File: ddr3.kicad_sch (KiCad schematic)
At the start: 26 parts, among them U11 LIFCL-40-9BG256C, U12 MT41K128M16JT-125_K

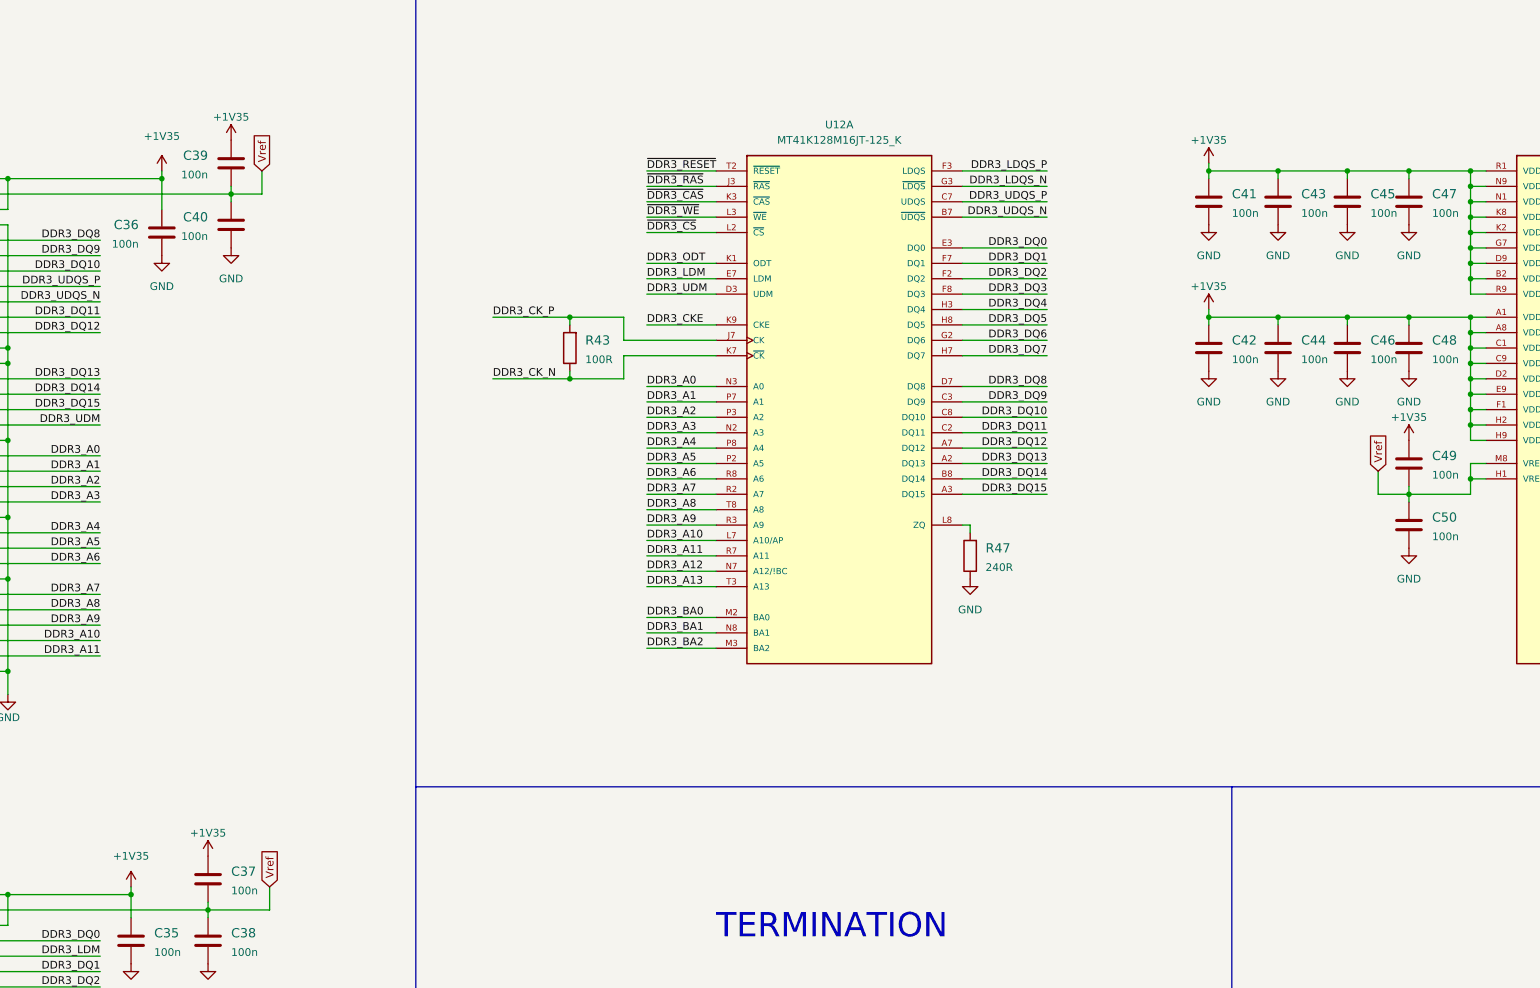
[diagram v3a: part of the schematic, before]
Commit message: Switched voltages to support DDR3 and RPC memories
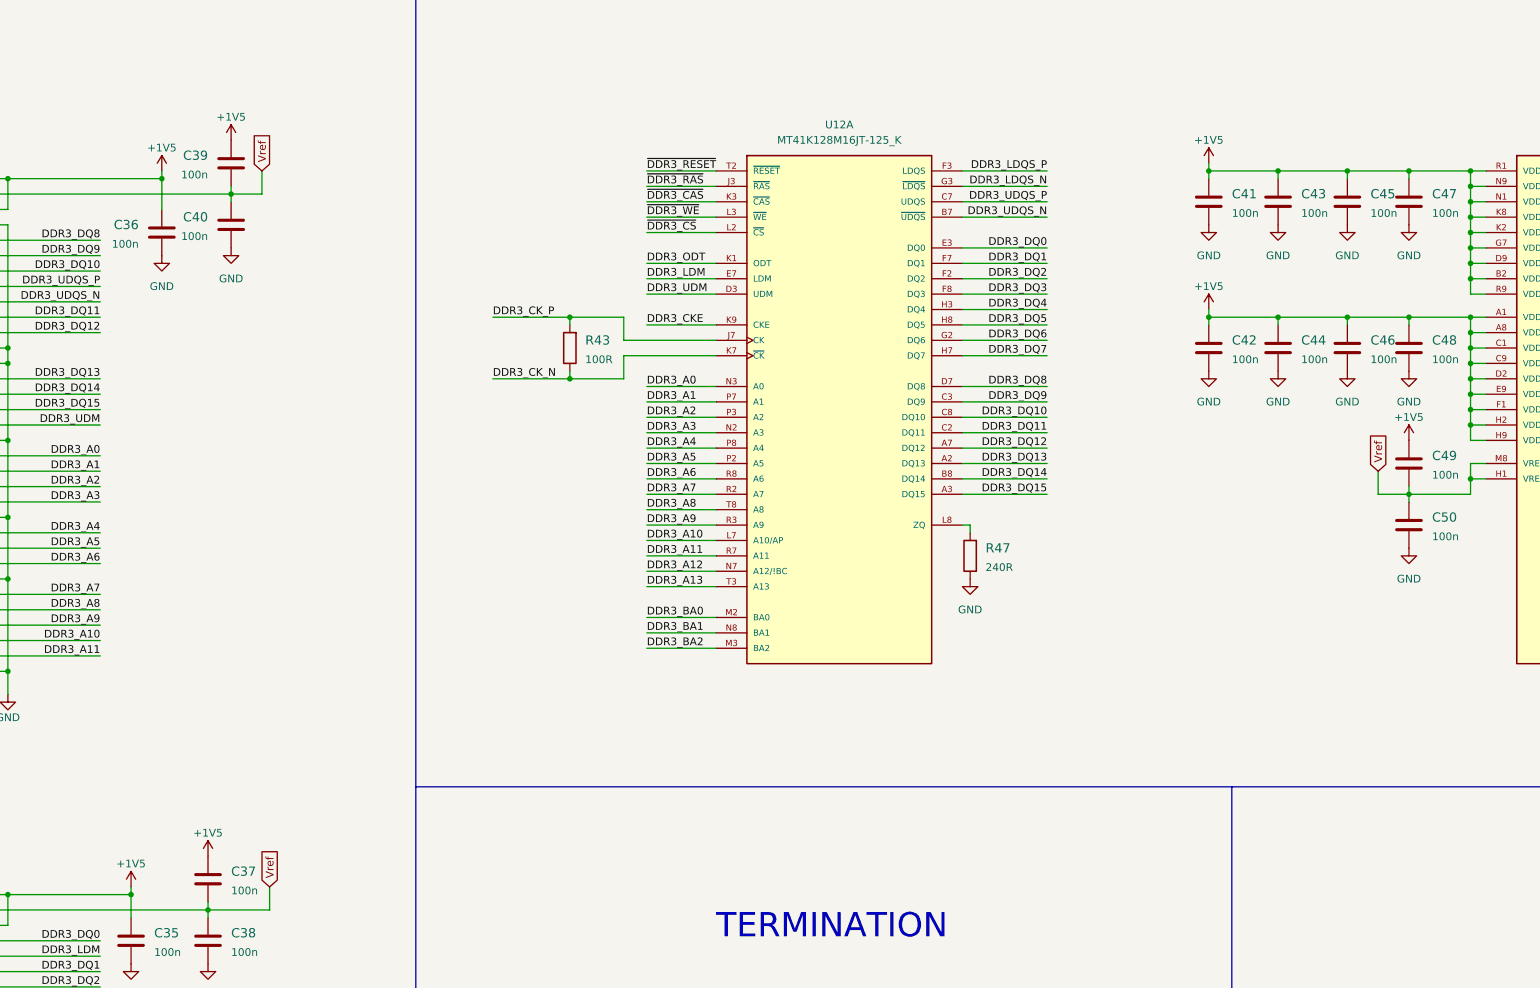
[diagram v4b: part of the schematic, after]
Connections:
- net +1V35 renamed +1V5
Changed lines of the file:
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@@
   (junction (at 269.24 207.01) (diameter 0) (color 0 0 0 0)
   )
-  (junction (at 295.91 78.74) (diameter 0) (color 0 0 0 0)
-  )
   (junction (at 226.06 209.55) (diameter 0) (color 0 0 0 0)
   )
@@
   (junction (at 339.09 54.61) (diameter 0) (color 0 0 0 0)
   )
+  (junction (at 295.91 78.74) (diameter 0) (color 0 0 0 0)
+  )
   (junction (at 269.24 226.06) (diameter 0) (color 0 0 0 0)
   )
@@
     (stroke (width 0) (type default) (color 0 0 0 0))
   )
+  (wire (pts (xy 295.91 77.47) (xy 295.91 78.74))
+    (stroke (width 0) (type default) (color 0 0 0 0))
+  )
   (wire (pts (xy 382.27 62.23) (xy 384.81 62.23))
     (stroke (width 0) (type default) (color 0 0 0 0))
@@
     (stroke (width 0) (type default) (color 0 0 0 0))
   )
-  (wire (pts (xy 295.91 77.47) (xy 295.91 78.74))
-    (stroke (width 0) (type default) (color 0 0 0 0))
-  )
   (wire (pts (xy 269.24 92.71) (xy 255.27 92.71))
     (stroke (width 0) (type default) (color 0 0 0 0))
@@
     (pin "2")
   )
-  (symbol (lib_id "power:+1V35") (at 295.91 77.47 0) (unit 1)
-    (in_bom yes) (on_board yes)
-    (property "Reference" "#PWR094" (id 0) (at 295.91 81.28 0)
-      (effects (font (size 1.27 1.27)) hide)
-    )
-    (property "Value" "+1V35" (id 1) (at 295.91 73.66 0))
-    (property "Footprint" "crosslink-nx-video-converter-footprints:" (id 2) (at 295.91 77.47 0)
-      (effects (font (size 1.27 1.27)) hide)
-    )
-    (property "Datasheet" "" (id 3) (at 295.91 77.47 0)
-      (effects (font (size 1.27 1.27)) hide)
-    )
-    (pin "1")
-  )
   (symbol (lib_id "power:GND") (at 307.34 63.5 0) (unit 1)
     (in_bom yes) (on_board yes) (fields_autoplaced)
@@
     (pin "8")
   )
-  (symbol (lib_id "power:+1V35") (at 328.93 99.06 0) (unit 1)
-    (in_bom yes) (on_board yes)
-    (property "Reference" "#PWR0102" (id 0) (at 328.93 102.87 0)
-      (effects (font (size 1.27 1.27)) hide)
-    )
-    (property "Value" "+1V35" (id 1) (at 328.93 95.25 0))
-    (property "Footprint" "crosslink-nx-video-converter-footprints:" (id 2) (at 328.93 99.06 0)
-      (effects (font (size 1.27 1.27)) hide)
-    )
-    (property "Datasheet" "" (id 3) (at 328.93 99.06 0)
-      (effects (font (size 1.27 1.27)) hide)
-    )
-    (pin "1")
-  )
   (symbol (lib_id "crosslink-nx-video-converter:R_100R_0402") (at 190.5 83.82 90) (unit 1)
     (in_bom yes) (on_board yes) (fields_autoplaced)
@@
     (pin "2")
   )
+  (symbol (lib_id "power:+1V5") (at 118.11 172.72 0) (unit 1)
+    (in_bom yes) (on_board yes)
+    (property "Reference" "#PWR0229" (id 0) (at 118.11 176.53 0)
+      (effects (font (size 1.27 1.27)) hide)
+    )
+    (property "Value" "+1V5" (id 1) (at 118.11 168.91 0))
+    (property "Footprint" "" (id 2) (at 118.11 172.72 0)
+      (effects (font (size 1.27 1.27)) hide)
+    )
+    (property "Datasheet" "" (id 3) (at 118.11 172.72 0)
+      (effects (font (size 1.27 1.27)) hide)
+    )
+    (pin "1")
+  )
   (symbol (lib_id "power:GND") (at 295.91 63.5 0) (unit 1)
     (in_bom yes) (on_board yes) (fields_autoplaced)
@@
     (pin "8")
   )
-  (symbol (lib_id "power:+1V35") (at 123.19 54.61 0) (mirror y) (unit 1)
-    (in_bom yes) (on_board yes) (fields_autoplaced)
-    (property "Reference" "#PWR085" (id 0) (at 123.19 58.42 0)
-      (effects (font (size 1.27 1.27)) hide)
-    )
-    (property "Value" "+1V35" (id 1) (at 123.19 48.895 0))
-    (property "Footprint" "crosslink-nx-video-converter-footprints:" (id 2) (at 123.19 54.61 0)
-      (effects (font (size 1.27 1.27)) hide)
-    )
-    (property "Datasheet" "" (id 3) (at 123.19 54.61 0)
-      (effects (font (size 1.27 1.27)) hide)
-    )
-    (pin "1")
-  )
   (symbol (lib_id "power:GND") (at 295.91 87.63 0) (unit 1)
     (in_bom yes) (on_board yes) (fields_autoplaced)
@@
     (pin "2")
   )
-  (symbol (lib_id "power:+1V35") (at 130.81 167.64 0) (mirror y) (unit 1)
+  (symbol (lib_id "power:+1V5") (at 130.81 167.64 0) (unit 1)
     (in_bom yes) (on_board yes)
-    (property "Reference" "#PWR087" (id 0) (at 130.81 171.45 0)
+    (property "Reference" "#PWR0230" (id 0) (at 130.81 171.45 0)
       (effects (font (size 1.27 1.27)) hide)
     )
-    (property "Value" "+1V35" (id 1) (at 130.81 163.83 0))
-    (property "Footprint" "crosslink-nx-video-converter-footprints:" (id 2) (at 130.81 167.64 0)
+    (property "Value" "+1V5" (id 1) (at 130.81 163.83 0))
+    (property "Footprint" "" (id 2) (at 130.81 167.64 0)
       (effects (font (size 1.27 1.27)) hide)
     )
@@
     (pin "2")
   )
+  (symbol (lib_id "power:+1V5") (at 134.62 49.53 0) (unit 1)
+    (in_bom yes) (on_board yes)
+    (property "Reference" "#PWR0231" (id 0) (at 134.62 53.34 0)
+      (effects (font (size 1.27 1.27)) hide)
+    )
+    (property "Value" "+1V5" (id 1) (at 134.62 45.72 0))
+    (property "Footprint" "" (id 2) (at 134.62 49.53 0)
+      (effects (font (size 1.27 1.27)) hide)
+    )
+    (property "Datasheet" "" (id 3) (at 134.62 49.53 0)
+      (effects (font (size 1.27 1.27)) hide)
+    )
+    (pin "1")
+  )
   (symbol (lib_id "crosslink-nx-video-converter:C_100n_0402") (at 307.34 59.69 0) (unit 1)
     (in_bom yes) (on_board yes) (fields_autoplaced)
@@
     (pin "2")
   )
+  (symbol (lib_id "power:+1V5") (at 328.93 99.06 0) (unit 1)
+    (in_bom yes) (on_board yes)
+    (property "Reference" "#PWR0234" (id 0) (at 328.93 102.87 0)
+      (effects (font (size 1.27 1.27)) hide)
+    )
+    (property "Value" "+1V5" (id 1) (at 328.93 95.25 0))
+    (property "Footprint" "" (id 2) (at 328.93 99.06 0)
+      (effects (font (size 1.27 1.27)) hide)
+    )
+    (property "Datasheet" "" (id 3) (at 328.93 99.06 0)
+      (effects (font (size 1.27 1.27)) hide)
+    )
+    (pin "1")
+  )
   (symbol (lib_id "power:GND") (at 118.11 185.42 0) (unit 1)
     (in_bom yes) (on_board yes) (fields_autoplaced)
@@
     (pin "1")
   )
-  (symbol (lib_id "power:+1V35") (at 118.11 172.72 0) (mirror y) (unit 1)
-    (in_bom yes) (on_board yes)
-    (property "Reference" "#PWR083" (id 0) (at 118.11 176.53 0)
-      (effects (font (size 1.27 1.27)) hide)
-    )
-    (property "Value" "+1V35" (id 1) (at 118.11 167.64 0))
-    (property "Footprint" "crosslink-nx-video-converter-footprints:" (id 2) (at 118.11 172.72 0)
-      (effects (font (size 1.27 1.27)) hide)
-    )
-    (property "Datasheet" "" (id 3) (at 118.11 172.72 0)
-      (effects (font (size 1.27 1.27)) hide)
-    )
-    (pin "1")
-  )
   (symbol (lib_id "power:GND") (at 97.79 140.97 0) (mirror y) (unit 1)
     (in_bom yes) (on_board yes)
@@
     (pin "2")
   )
-  (symbol (lib_id "power:+1V35") (at 295.91 53.34 0) (unit 1)
-    (in_bom yes) (on_board yes)
-    (property "Reference" "#PWR092" (id 0) (at 295.91 57.15 0)
-      (effects (font (size 1.27 1.27)) hide)
-    )
-    (property "Value" "+1V35" (id 1) (at 295.91 49.53 0))
-    (property "Footprint" "crosslink-nx-video-converter-footprints:" (id 2) (at 295.91 53.34 0)
-      (effects (font (size 1.27 1.27)) hide)
-    )
-    (property "Datasheet" "" (id 3) (at 295.91 53.34 0)
-      (effects (font (size 1.27 1.27)) hide)
-    )
-    (pin "1")
-  )
   (symbol (lib_id "power:GND") (at 307.34 87.63 0) (unit 1)
     (in_bom yes) (on_board yes) (fields_autoplaced)
@@
     (pin "8")
   )
-  (symbol (lib_id "power:+1V35") (at 134.62 49.53 0) (mirror y) (unit 1)
-    (in_bom yes) (on_board yes)
-    (property "Reference" "#PWR089" (id 0) (at 134.62 53.34 0)
-      (effects (font (size 1.27 1.27)) hide)
-    )
-    (property "Value" "+1V35" (id 1) (at 134.62 45.72 0))
-    (property "Footprint" "crosslink-nx-video-converter-footprints:" (id 2) (at 134.62 49.53 0)
-      (effects (font (size 1.27 1.27)) hide)
-    )
-    (property "Datasheet" "" (id 3) (at 134.62 49.53 0)
-      (effects (font (size 1.27 1.27)) hide)
-    )
-    (pin "1")
-  )
   (symbol (lib_id "power:GND") (at 328.93 63.5 0) (unit 1)
     (in_bom yes) (on_board yes) (fields_autoplaced)
@@
     (pin "1")
   )
+  (symbol (lib_id "power:+1V5") (at 295.91 77.47 0) (unit 1)
+    (in_bom yes) (on_board yes)
+    (property "Reference" "#PWR0233" (id 0) (at 295.91 81.28 0)
+      (effects (font (size 1.27 1.27)) hide)
+    )
+    (property "Value" "+1V5" (id 1) (at 295.91 73.66 0))
+    (property "Footprint" "" (id 2) (at 295.91 77.47 0)
+      (effects (font (size 1.27 1.27)) hide)
+    )
+    (property "Datasheet" "" (id 3) (at 295.91 77.47 0)
+      (effects (font (size 1.27 1.27)) hide)
+    )
+    (pin "1")
+  )
   (symbol (lib_id "power:GND") (at 134.62 67.31 0) (mirror y) (unit 1)
     (in_bom yes) (on_board yes) (fields_autoplaced)
@@
     (pin "T9")
   )
+  (symbol (lib_id "power:+1V5") (at 295.91 53.34 0) (unit 1)
+    (in_bom yes) (on_board yes)
+    (property "Reference" "#PWR0235" (id 0) (at 295.91 57.15 0)
+      (effects (font (size 1.27 1.27)) hide)
+    )
+    (property "Value" "+1V5" (id 1) (at 295.91 49.53 0))
+    (property "Footprint" "" (id 2) (at 295.91 53.34 0)
+      (effects (font (size 1.27 1.27)) hide)
+    )
+    (property "Datasheet" "" (id 3) (at 295.91 53.34 0)
+      (effects (font (size 1.27 1.27)) hide)
+    )
+    (pin "1")
+  )
+  (symbol (lib_id "power:+1V5") (at 123.19 54.61 0) (unit 1)
+    (in_bom yes) (on_board yes)
+    (property "Reference" "#PWR0232" (id 0) (at 123.19 58.42 0)
+      (effects (font (size 1.27 1.27)) hide)
+    )
+    (property "Value" "+1V5" (id 1) (at 123.19 50.8 0))
+    (property "Footprint" "" (id 2) (at 123.19 54.61 0)
+      (effects (font (size 1.27 1.27)) hide)
+    )
+    (property "Datasheet" "" (id 3) (at 123.19 54.61 0)
+      (effects (font (size 1.27 1.27)) hide)
+    )
+    (pin "1")
+  )
 )

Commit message: Placed components
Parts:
- C16: renamed from C35; value C_100n_0603 -> C_100n_0402; footprint crosslink-nx-video-converter-footprints:0603-cap -> antmicro-footprints:0402-cap; symbol crosslink-nx-video-converter:C_100n_0603 -> antmicroCapacitors0402:C_100n_0402; MPN 0603YC104KAZ2A -> GRM155R61H104KE14D; Manufacturer AVX -> Murata
- C35: renamed from C36; value C_100n_0603 -> C_100n_0402; footprint crosslink-nx-video-converter-footprints:0603-cap -> antmicro-footprints:0402-cap; symbol crosslink-nx-video-converter:C_100n_0603 -> antmicroCapacitors0402:C_100n_0402; MPN 0603YC104KAZ2A -> GRM155R61H104KE14D; Manufacturer AVX -> Murata
- C36: renamed from C37; value C_100n_0603 -> C_100n_0402; footprint crosslink-nx-video-converter-footprints:0603-cap -> antmicro-footprints:0402-cap; symbol crosslink-nx-video-converter:C_100n_0603 -> antmicroCapacitors0402:C_100n_0402; MPN 0603YC104KAZ2A -> GRM155R61H104KE14D; Manufacturer AVX -> Murata
- C37: renamed from C38; value C_100n_0603 -> C_100n_0402; footprint crosslink-nx-video-converter-footprints:0603-cap -> antmicro-footprints:0402-cap; symbol crosslink-nx-video-converter:C_100n_0603 -> antmicroCapacitors0402:C_100n_0402; MPN 0603YC104KAZ2A -> GRM155R61H104KE14D; Manufacturer AVX -> Murata
- C38: renamed from C39; value C_100n_0603 -> C_100n_0402; footprint crosslink-nx-video-converter-footprints:0603-cap -> antmicro-footprints:0402-cap; symbol crosslink-nx-video-converter:C_100n_0603 -> antmicroCapacitors0402:C_100n_0402; MPN 0603YC104KAZ2A -> GRM155R61H104KE14D; Manufacturer AVX -> Murata
- C39: renamed from C40; value C_100n_0603 -> C_100n_0402; footprint crosslink-nx-video-converter-footprints:0603-cap -> antmicro-footprints:0402-cap; symbol crosslink-nx-video-converter:C_100n_0603 -> antmicroCapacitors0402:C_100n_0402; MPN 0603YC104KAZ2A -> GRM155R61H104KE14D; Manufacturer AVX -> Murata
